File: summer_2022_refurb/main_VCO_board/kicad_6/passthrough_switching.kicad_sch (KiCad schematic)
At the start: 4 parts, among them U10 DG413xY, U9 LM555xM

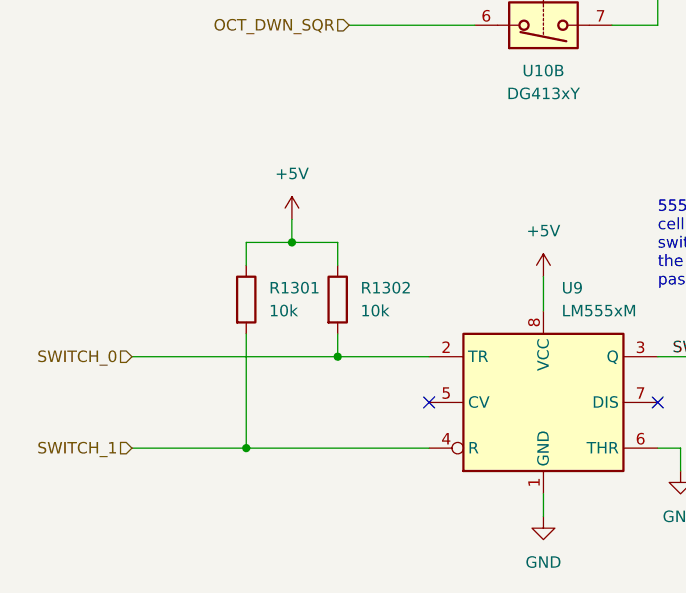
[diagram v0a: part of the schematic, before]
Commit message: Fix VCO issues, suboct switching, component values
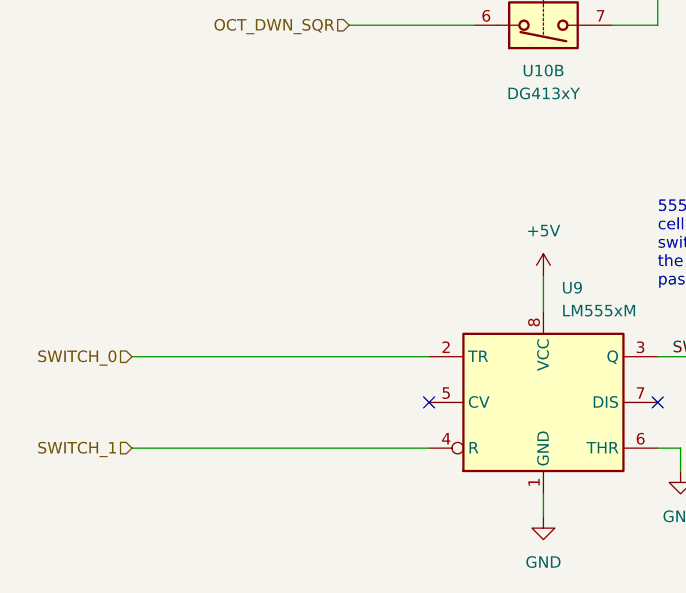
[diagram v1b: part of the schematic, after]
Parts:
- removed R1301, R1302: 10k, Resistor_SMD:R_0805_2012Metric, symbol Device:R
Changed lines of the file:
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@@
   (title_block
     (title "Josh Ox Ribon Synth Main VCO board")
-    (date "2022-06-18")
-    (rev "0")
+    (date "2022-07-07")
+    (rev "0.1")
     (comment 2 "creativecommons.org/licences/by/4.0")
     (comment 3 "license: CC by 4.0")
     (comment 4 "Author: Jordan Acete")
   )
-  (junction (at 125.73 120.65) (diameter 0) (color 0 0 0 0)
-  )
   (junction (at 166.37 87.63) (diameter 0) (color 0 0 0 0)
   )
-  (junction (at 130.81 133.35) (diameter 0) (color 0 0 0 0)
-  )
   (junction (at 153.67 48.26) (diameter 0) (color 0 0 0 0)
   )
   (junction (at 165.1 48.26) (diameter 0) (color 0 0 0 0)
-  )
-  (junction (at 120.65 143.51) (diameter 0) (color 0 0 0 0)
   )
   (junction (at 153.67 87.63) (diameter 0) (color 0 0 0 0)
@@
     (stroke (width 0) (type default) (color 0 0 0 0))
   )
-  (wire (pts (xy 140.97 143.51) (xy 120.65 143.51))
+  (wire (pts (xy 107.95 143.51) (xy 140.97 143.51))
     (stroke (width 0) (type default) (color 0 0 0 0))
   )
@@
     (stroke (width 0) (type default) (color 0 0 0 0))
   )
-  (wire (pts (xy 140.97 133.35) (xy 130.81 133.35))
-    (stroke (width 0) (type default) (color 0 0 0 0))
-  )
-  (wire (pts (xy 130.81 120.65) (xy 125.73 120.65))
-    (stroke (width 0) (type default) (color 0 0 0 0))
-  )
   (wire (pts (xy 161.29 55.88) (xy 165.1 55.88))
     (stroke (width 0) (type default) (color 0 0 0 0))
@@
     (stroke (width 0) (type default) (color 0 0 0 0))
   )
-  (wire (pts (xy 130.81 133.35) (xy 130.81 130.81))
-    (stroke (width 0) (type default) (color 0 0 0 0))
-  )
-  (wire (pts (xy 107.95 143.51) (xy 120.65 143.51))
-    (stroke (width 0) (type default) (color 0 0 0 0))
-  )
   (wire (pts (xy 168.91 143.51) (xy 168.91 146.05))
     (stroke (width 0) (type default) (color 0 0 0 0))
@@
     (stroke (width 0) (type default) (color 0 0 0 0))
   )
-  (wire (pts (xy 130.81 123.19) (xy 130.81 120.65))
-    (stroke (width 0) (type default) (color 0 0 0 0))
-  )
   (wire (pts (xy 153.67 48.26) (xy 153.67 50.8))
     (stroke (width 0) (type default) (color 0 0 0 0))
   )
-  (wire (pts (xy 107.95 133.35) (xy 130.81 133.35))
+  (wire (pts (xy 107.95 133.35) (xy 140.97 133.35))
     (stroke (width 0) (type default) (color 0 0 0 0))
   )
@@
     (stroke (width 0) (type default) (color 0 0 0 0))
   )
-  (wire (pts (xy 125.73 118.11) (xy 125.73 120.65))
-    (stroke (width 0) (type default) (color 0 0 0 0))
-  )
-  (wire (pts (xy 120.65 120.65) (xy 120.65 123.19))
-    (stroke (width 0) (type default) (color 0 0 0 0))
-  )
   (wire (pts (xy 153.67 87.63) (xy 153.67 91.44))
     (stroke (width 0) (type default) (color 0 0 0 0))
@@
   )
   (wire (pts (xy 166.37 133.35) (xy 179.07 133.35))
-    (stroke (width 0) (type default) (color 0 0 0 0))
-  )
-  (wire (pts (xy 125.73 120.65) (xy 120.65 120.65))
-    (stroke (width 0) (type default) (color 0 0 0 0))
-  )
-  (wire (pts (xy 120.65 143.51) (xy 120.65 130.81))
     (stroke (width 0) (type default) (color 0 0 0 0))
   )
@@
     (pin "5")
   )
-  (symbol (lib_id "power:+5V") (at 125.73 118.11 0) (unit 1)
-    (in_bom yes) (on_board yes) (fields_autoplaced)
-    (property "Reference" "#PWR01301" (id 0) (at 125.73 121.92 0)
-      (effects (font (size 1.27 1.27)) hide)
-    )
-    (property "Value" "+5V" (id 1) (at 125.73 113.03 0))
-    (property "Footprint" "" (id 2) (at 125.73 118.11 0)
-      (effects (font (size 1.27 1.27)) hide)
-    )
-    (property "Datasheet" "" (id 3) (at 125.73 118.11 0)
-      (effects (font (size 1.27 1.27)) hide)
-    )
-    (pin "1")
-  )
   (symbol (lib_id "Analog_Switch:DG413xY") (at 153.67 78.74 0) (unit 3)
     (in_bom yes) (on_board yes) (fields_autoplaced)
@@
     (pin "7")
   )
-  (symbol (lib_id "Device:R") (at 120.65 127 0) (unit 1)
-    (in_bom yes) (on_board yes) (fields_autoplaced)
-    (property "Reference" "R1301" (id 0) (at 123.19 125.7299 0)
-      (effects (font (size 1.27 1.27)) (justify left))
-    )
-    (property "Value" "10k" (id 1) (at 123.19 128.2699 0)
-      (effects (font (size 1.27 1.27)) (justify left))
-    )
-    (property "Footprint" "Resistor_SMD:R_0805_2012Metric" (id 2) (at 118.872 127 90)
-      (effects (font (size 1.27 1.27)) hide)
-    )
-    (property "Datasheet" "~" (id 3) (at 120.65 127 0)
-      (effects (font (size 1.27 1.27)) hide)
-    )
-    (pin "1")
-    (pin "2")
-  )
   (symbol (lib_id "power:GND") (at 153.67 151.13 0) (unit 1)
     (in_bom yes) (on_board yes) (fields_autoplaced)
@@
     (pin "1")
   )
-  (symbol (lib_id "Device:R") (at 130.81 127 0) (unit 1)
-    (in_bom yes) (on_board yes) (fields_autoplaced)
-    (property "Reference" "R1302" (id 0) (at 133.35 125.7299 0)
-      (effects (font (size 1.27 1.27)) (justify left))
-    )
-    (property "Value" "10k" (id 1) (at 133.35 128.2699 0)
-      (effects (font (size 1.27 1.27)) (justify left))
-    )
-    (property "Footprint" "Resistor_SMD:R_0805_2012Metric" (id 2) (at 129.032 127 90)
-      (effects (font (size 1.27 1.27)) hide)
-    )
-    (property "Datasheet" "~" (id 3) (at 130.81 127 0)
-      (effects (font (size 1.27 1.27)) hide)
-    )
-    (pin "1")
-    (pin "2")
-  )
 )
